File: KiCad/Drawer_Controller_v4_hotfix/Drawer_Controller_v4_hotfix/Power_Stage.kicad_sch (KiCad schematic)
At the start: 23 parts, among them U12 LM1117MPX-3.3-NOPB, U3 LMR33630

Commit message: feat: updates `Drawer_Controller_v4_hotfix` and `Partial_Drawer_Controller_v1_hotfix` with newest docs
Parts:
- C4, C5, C6: path_to_docs (none) -> Passive_Components/Capacitors/MLCC/FH
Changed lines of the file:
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@@
 			)
 		)
-		(property "Datasheet" "~"
+		(property "Datasheet" "https://www.lcsc.com/datasheet/lcsc_datasheet_2304140030_FH--Guangdong-Fenghua-Advanced-Tech-1206B475K500NT_C29823.pdf"
 			(at 123.19 50.8 0)
 			(effects
@@
 			)
 		)
+		(property "OC_CONRAD" ""
+			(at 123.19 50.8 0)
+			(effects
+				(font
+					(size 1.27 1.27)
+				)
+				(hide yes)
+			)
+		)
+		(property "OC_RS" ""
+			(at 123.19 50.8 0)
+			(effects
+				(font
+					(size 1.27 1.27)
+				)
+				(hide yes)
+			)
+		)
+		(property "path_to_docs" "Passive_Components/Capacitors/MLCC/FH"
+			(at 123.19 50.8 0)
+			(effects
+				(font
+					(size 1.27 1.27)
+				)
+				(hide yes)
+			)
+		)
 		(pin "2"
 		)
@@
 			)
 		)
-		(property "Datasheet" "~"
+		(property "Datasheet" "https://www.lcsc.com/datasheet/lcsc_datasheet_2304140030_FH--Guangdong-Fenghua-Advanced-Tech-1206B475K500NT_C29823.pdf"
 			(at 92.71 50.8 0)
 			(effects
@@
 			)
 		)
+		(property "OC_CONRAD" ""
+			(at 92.71 50.8 0)
+			(effects
+				(font
+					(size 1.27 1.27)
+				)
+				(hide yes)
+			)
+		)
+		(property "OC_RS" ""
+			(at 92.71 50.8 0)
+			(effects
+				(font
+					(size 1.27 1.27)
+				)
+				(hide yes)
+			)
+		)
+		(property "path_to_docs" "Passive_Components/Capacitors/MLCC/FH"
+			(at 92.71 50.8 0)
+			(effects
+				(font
+					(size 1.27 1.27)
+				)
+				(hide yes)
+			)
+		)
 		(pin "2"
 		)
@@
 			)
 		)
-		(property "Datasheet" "~"
+		(property "Datasheet" "https://www.lcsc.com/datasheet/lcsc_datasheet_2304140030_FH--Guangdong-Fenghua-Advanced-Tech-1206B475K500NT_C29823.pdf"
 			(at 108.585 50.8 0)
 			(effects
@@
 			(at 108.585 50.8 0)
 			(effects
+				(font
+					(size 1.27 1.27)
+				)
+				(hide yes)
+			)
+		)
+		(property "OC_CONRAD" ""
+			(at 108.585 50.8 0)
+			(effects
+				(font
+					(size 1.27 1.27)
+				)
+				(hide yes)
+			)
+		)
+		(property "OC_RS" ""
+			(at 108.585 50.8 0)
+			(effects
+				(font
+					(size 1.27 1.27)
+				)
+				(hide yes)
+			)
+		)
+		(property "path_to_docs" "Passive_Components/Capacitors/MLCC/FH"
+			(at 108.585 50.8 0)
+			(effects

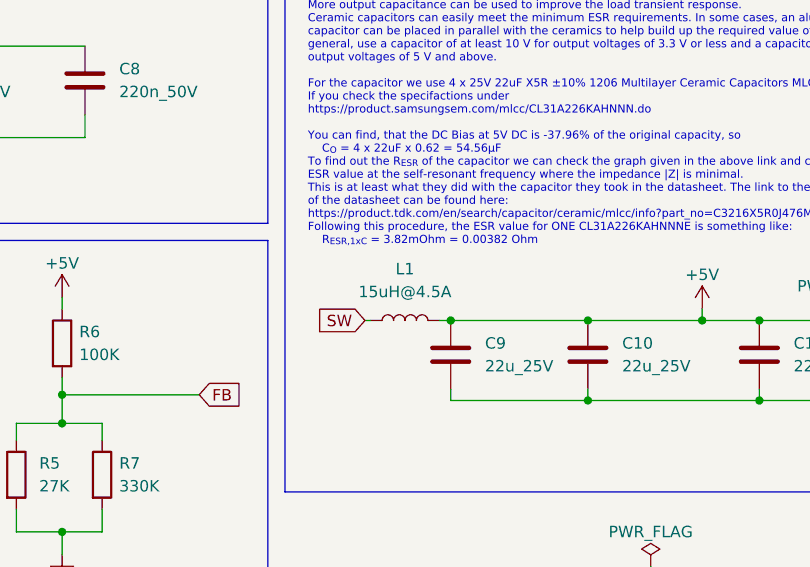
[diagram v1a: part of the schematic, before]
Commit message: feat: updates `Drawer_Controller_v4_hotfix` and `Partial_Drawer_Controller_v1_hotfix` with power inductor that has documents
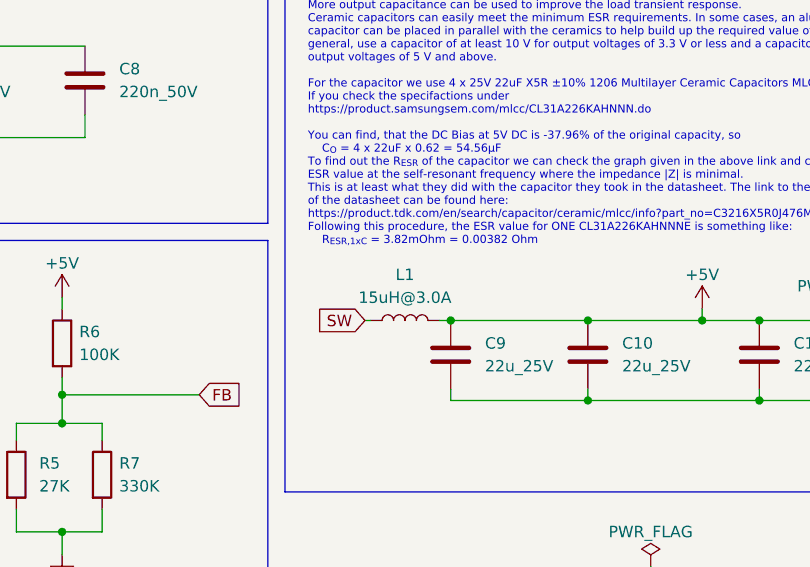
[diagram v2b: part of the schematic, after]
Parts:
- removed L1: 15uH@4.5A, Robast:Power_Inductor_SMDRI127, symbol _L_Power:15uH@4.5A
- added L1: 15uH@3.0A, Robast:IND_ETQP3M150KVN, symbol _L_Power:15uH@3.0A
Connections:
- net +5V: now also L1.2
- net SW: now also L1.1
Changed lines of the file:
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@@
+	)
+	(symbol
+		(lib_id "_L_Power:15uH@3.0A")
+		(at 177.8 77.47 90)
+		(unit 1)
+		(exclude_from_sim no)
+		(in_bom yes)
+		(on_board yes)
+		(dnp no)
+		(fields_autoplaced yes)
+		(property "Reference" "L1"
+			(at 177.8 72.39 90)
+			(effects
+				(font
+					(size 1.27 1.27)
+				)
+			)
+		)
+		(property "Value" "15uH@3.0A"
+			(at 177.8 74.93 90)
+			(effects
+				(font
+					(size 1.27 1.27)
+				)
+			)
+		)
+		(property "Footprint" "Robast:IND_ETQP3M150KVN"
+			(at 177.8 77.47 0)
+			(effects
+				(font
+					(size 1.27 1.27)
+				)
+				(hide yes)
+			)
+		)
+		(property "Datasheet" "https://www.mouser.de/datasheet/2/315/AGL0000C63-1283966.pdf"
+			(at 177.8 77.47 0)
+			(effects
+				(font
+					(size 1.27 1.27)
+				)
+				(hide yes)
+			)
+		)
+		(property "Description" "Integrated Polded Power Inductor 15uH@3.0A, 0.099Ω, I_SAT=5.1"
+			(at 177.8 77.47 0)
+			(effects
+				(font
+					(size 1.27 1.27)
+				)
+				(hide yes)
+			)
+		)
+		(property "MF" "PANASONIC"
+			(at 177.8 77.47 0)
+			(effects
+				(font
+					(size 1.27 1.27)
+				)
+				(hide yes)
+			)
+		)
+		(property "MPN" "ETQP3M150KVN"
+			(at 177.8 77.47 0)
+			(effects
+				(font
+					(size 1.27 1.27)
+				)
+				(hide yes)
+			)
+		)
+		(property "OC_CONRAD" ""
+			(at 177.8 77.47 0)
+			(effects
+				(font
+					(size 1.27 1.27)
+				)
+				(hide yes)
+			)
+		)
+		(property "OC_LCSC" "C542310"
+			(at 177.8 77.47 0)
+			(effects
+				(font
+					(size 1.27 1.27)
+				)
+				(hide yes)
+			)
+		)
+		(property "OC_MOUSER" "667-ETQ-P3M150KVN"
+			(at 177.8 77.47 0)
+			(effects
+				(font
+					(size 1.27 1.27)
+				)
+				(hide yes)
+			)
+		)
+		(property "OC_RS" "238-3570"
+			(at 177.8 77.47 0)
+			(effects
+				(font
+					(size 1.27 1.27)
+				)
+				(hide yes)
+			)
+		)
+		(property "path_to_docs" "Passive_Components/Inductors/Power_Inductors_SMD/Panasonic"
+			(at 177.8 77.47 0)
+			(effects
+				(font
+					(size 1.27 1.27)
+				)
+				(hide yes)
+			)
+		)
+		(pin "1"
+		)
+		(pin "2"
+		)
+		(instances
+			(project ""
+				(path "/57f8c193-fe09-43d3-9441-dbd40881d2aa/cf52d563-fbeb-48d6-b236-fc325e3d0bb7"
+					(reference "L1")
+					(unit 1)
+				)
+			)
+		)
 	)
 	(symbol
@@
 					(unit 1)
 				)
-			)
-		)
-	)
-	(symbol
-		(lib_id "_L_Power:15uH@4.5A")
-		(at 177.8 77.47 90)
-		(unit 1)
-		(exclude_from_sim no)
-		(in_bom yes)
-		(on_board yes)
-		(dnp no)
-		(fields_autoplaced yes)
-		(property "Reference" "L1"
-			(at 177.8 71.755 90)
-			(effects
-				(font
-					(size 1.27 1.27)
-				)
-			)
-		)
-		(property "Value" "15uH@4.5A"
-			(at 177.8 74.295 90)
-			(effects
-				(font
-					(size 1.27 1.27)
-				)
-			)
-		)
-		(property "Footprint" "Robast:Power_Inductor_SMDRI127"
-			(at 177.8 77.47 0)
-			(effects
-				(font
-					(size 1.27 1.27)
-				)
-				(hide yes)
-			)
-		)
-		(property "Datasheet" "https://datasheet.lcsc.com/lcsc/2108131530_SXN-Shun-Xiang-Nuo-Elec-SMDRI127-150MT_C40000.pdf"
-			(at 177.8 77.47 0)
-			(effects
-				(font
-					(size 1.27 1.27)
-				)
-				(hide yes)
-			)
-		)
-		(property "Description" "Shielded Power Inductor 15uH@4.5A, 0.027Ω, I_SAT=8A"
-			(at 177.8 77.47 0)
-			(effects
-				(font
-					(size 1.27 1.27)
-				)
-				(hide yes)
-			)
-		)
-		(property "MF" "SXN(Shun Xiang Nuo Elec)"
-			(at 177.8 77.47 0)
-			(effects
-				(font
-					(size 1.27 1.27)
-				)
-				(hide yes)
-			)
-		)
-		(property "MPN" "SMDRI127-150MT"
-			(at 177.8 77.47 0)
-			(effects
-				(font
-					(size 1.27 1.27)
-				)
-				(hide yes)
-			)
-		)
-		(property "OC_LCSC" "C40000"
-			(at 177.8 77.47 0)
-			(effects
-				(font
-					(size 1.27 1.27)
-				)
-				(hide yes)
-			)
-		)
-		(property "OC_MOUSER" ""
-			(at 177.8 77.47 0)
-			(effects
-				(font
-					(size 1.27 1.27)
-				)
-				(hide yes)
-			)
-		)
-		(pin "1"
-		)
-		(pin "2"
-		)
-		(instances
-			(project "Drawer_Controller_v4"
-				(path "/57f8c193-fe09-43d3-9441-dbd40881d2aa/cf52d563-fbeb-48d6-b236-fc325e3d0bb7"
-					(reference "L1")
-					(unit 1)
-				)
